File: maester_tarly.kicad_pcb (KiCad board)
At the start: 4 copper layers, 72 x 62.4 mm, 126 parts, among them J101 Micro_SD_Card_Det, J102 USB_B_Micro, J103 USB_A, J104 Conn_01x06, J105 Conn_01x10, J106 RJ45_Amphenol_RJMG1BD3B8K1ANR, J107 DF40GB(1.5)-48DS-0.4V, J108 DF40GB(1.5)-48DS-0.4V, J109 DF40GB(1.5)-48DS-0.4V, J110 DF40GB(1.5)-48DS-0.4V, U1 SAM9X60, U2 W971GG6SB-18, U3 MCP16501, U501 KSZ8081RNA, Y401 32.768kHz, Y402 DSC1001, Y501 DSC1001

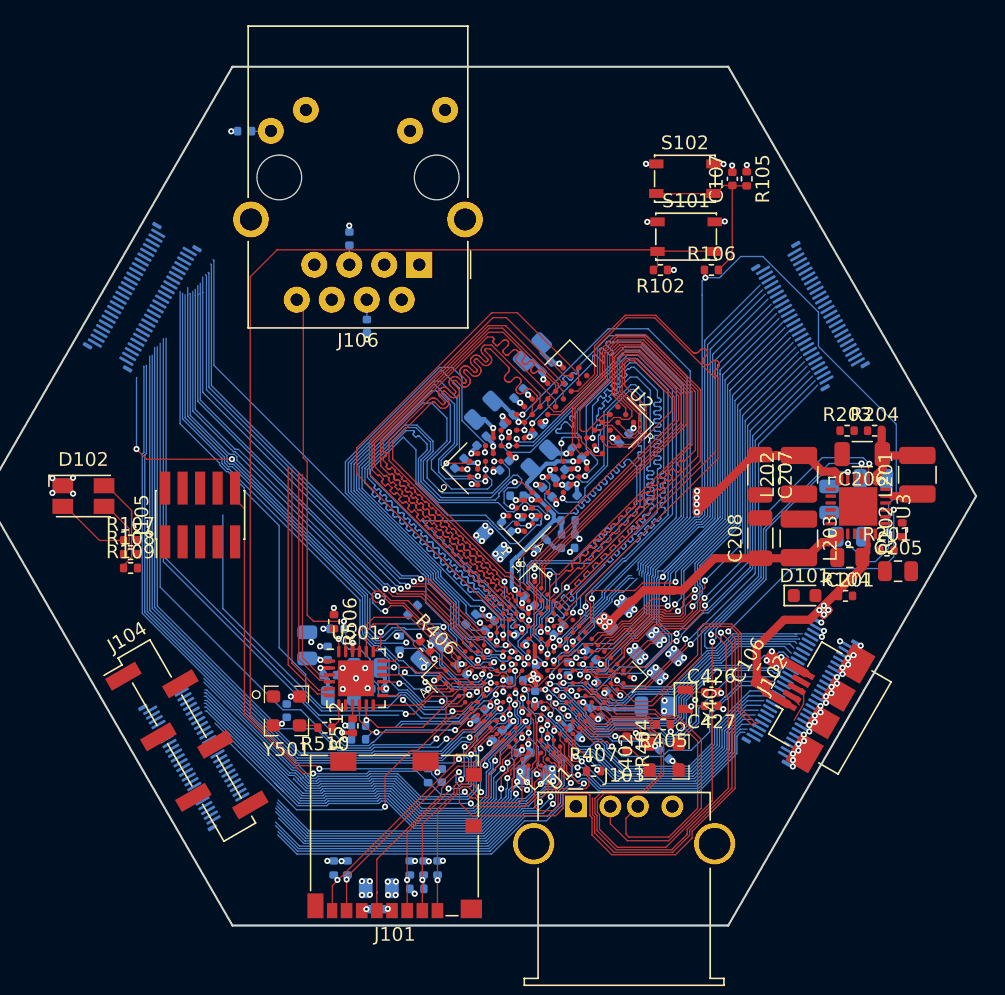
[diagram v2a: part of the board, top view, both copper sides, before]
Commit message: Routed power supply traces and vias. Repositioned mezzanine connectors.
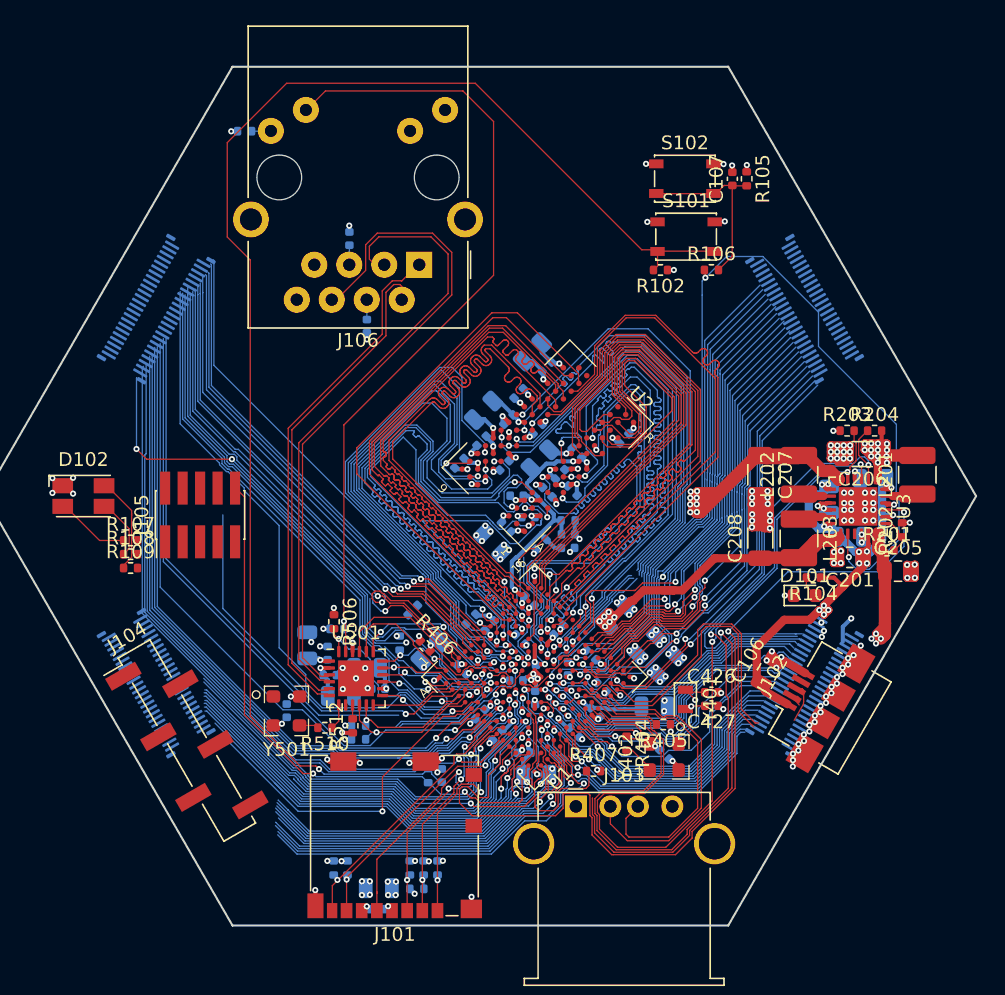
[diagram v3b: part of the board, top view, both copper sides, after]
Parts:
- moved J107 6.09 mm to (94.5, 144.8)
- moved R104 2.68 mm to (142.2, 137.1), turned to 180 degrees
- moved J109 1.33 mm to (94.5, 117.6)
- moved J110 0.67 mm to (141.5, 117.6)
- moved J108 0.66 mm to (141.5, 144.8)
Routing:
- net /ldo_out: track 0.00 -> 75.9 mm, vias 0 -> 4
- net GND: track 72.4 -> 129.1 mm, vias 126 -> 188
- net /a24: track 52.9 -> 15.1 mm
- net /a23: track 55.4 -> 92.9 mm
- net +5V: track 105.3 -> 139.7 mm, vias 4 -> 15
- net /CPU_IO/CPU_ETH_RX_N: track 15.9 -> 48.9 mm
- net /CPU_IO/CPU_ETH_LED: track 28.6 -> 58.8 mm
- net /CPU_IO/CPU_ETH_RX_P: track 16.4 -> 45.5 mm
- net /CPU_IO/CPU_ETH_TX_P: track 18.1 -> 37.2 mm
- net Net-(C105-Pad1): track 84.0 -> 102.5 mm
- net /CPU_IO/CPU_ETH_TX_N: track 17.7 -> 35.7 mm
- net +1.8V: track 50.7 -> 67.9 mm, vias 28 -> 32
- net +1.15V: track 41.4 -> 51.1 mm, vias 7 -> 9
- net +3V3: track 36.4 -> 45.9 mm, vias 50 -> 64
- net Net-(L202-Pad1): track 0.00 -> 3.52 mm
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
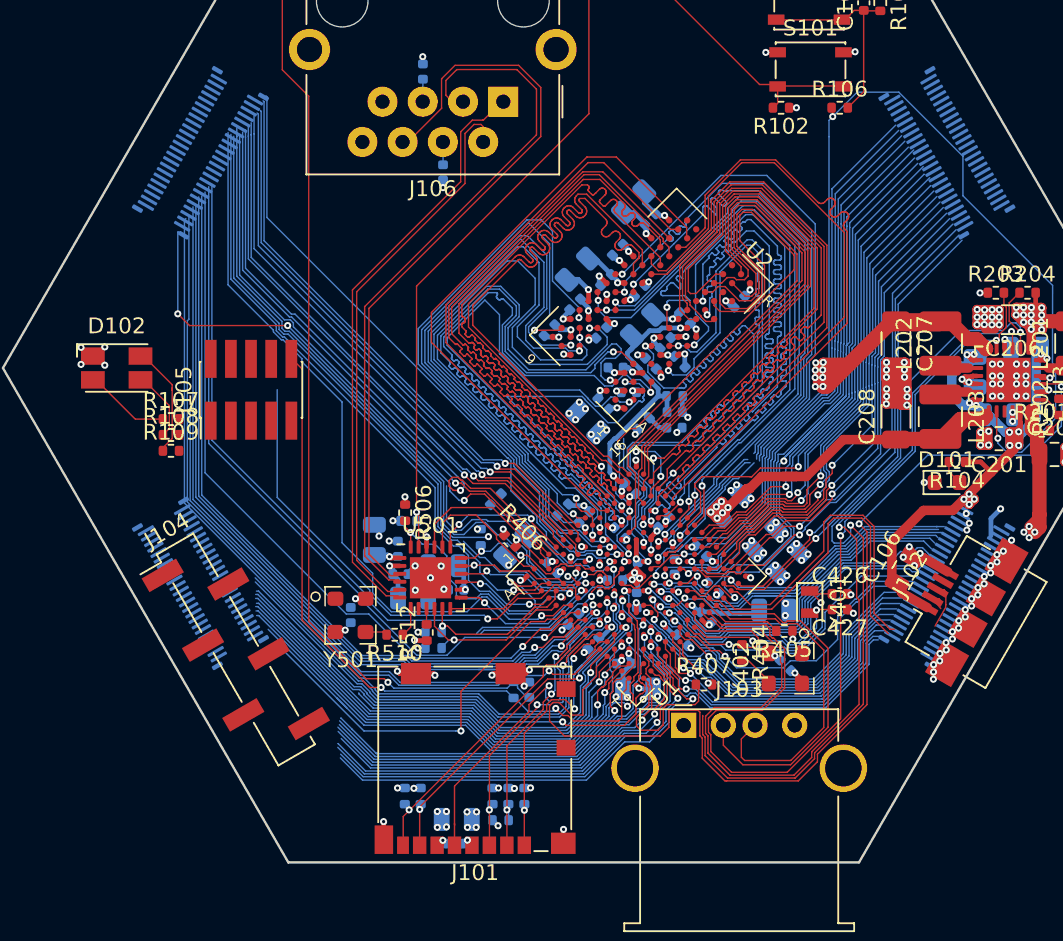
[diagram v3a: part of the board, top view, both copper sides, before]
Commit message: Wired up J107 and J109
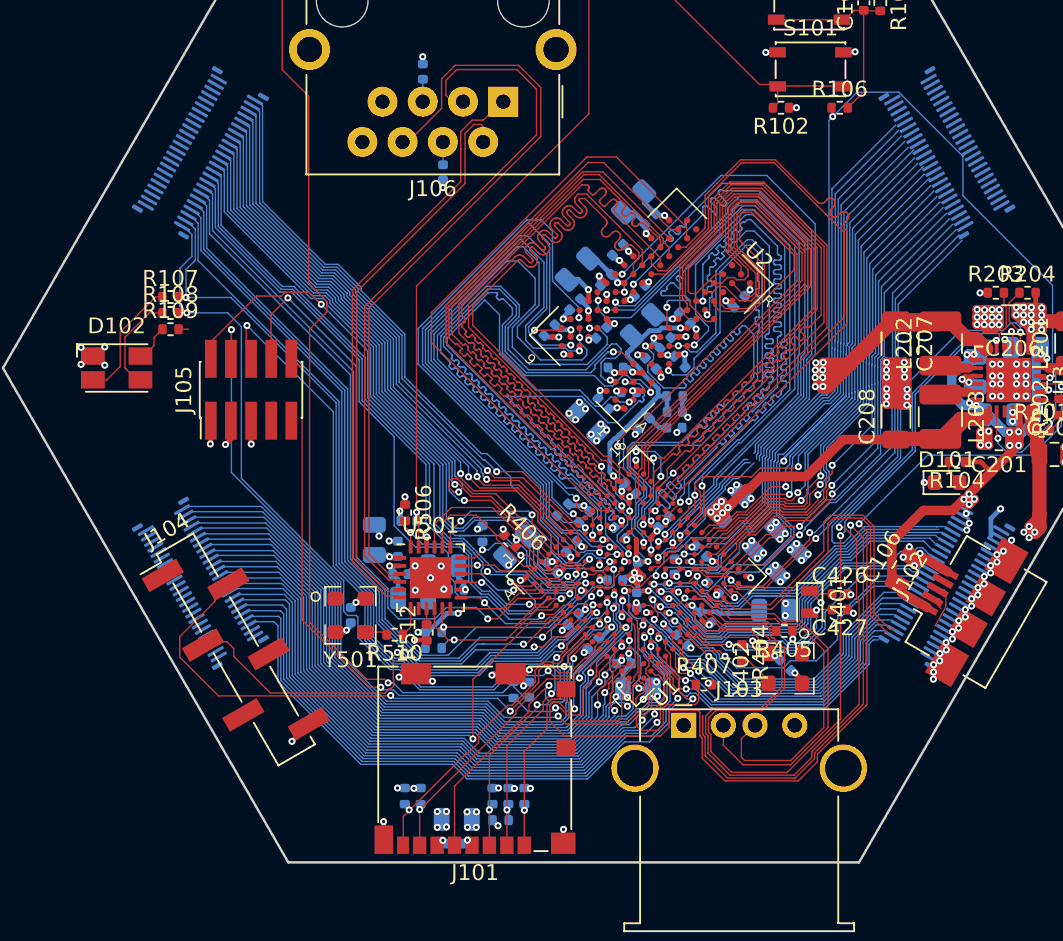
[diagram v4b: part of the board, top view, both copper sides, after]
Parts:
- moved R107 7.70 mm to (92.6, 126.7)
- moved R108 7.69 mm to (92.6, 127.7)
- moved R109 7.67 mm to (92.6, 128.7)
- moved C424 5.63 mm to (117.9, 142.4)
- moved R507 0.25 mm to (112.2, 141.6)
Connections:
- J107 pad 10: /c2 -> /c5
- J107 pad 12: /c3 -> /c7
- J107 pad 14: /c4 -> /c1
- J107 pad 16: /c5 -> /c3
- J107 pad 18: /c6 -> /c2
- J107 pad 20: /c7 -> /c6
- J107 pad 22: /c8 -> /c0
- J107 pad 24: /c9 -> /c4
- J107 pad 26: /a21 -> /a28
- J107 pad 28: /a14 -> /a7
- J107 pad 30: /a13 -> /a1
- J107 pad 32: /a12 -> /a2
- J107 pad 34: /a7 -> /a0
- J107 pad 36: /a6 -> /a4
- J107 pad 38: /a5 -> /a6
- J107 pad 40: /a4 -> /a13
- J107 pad 44: /a2 -> /a5
- J107 pad 46: /a1 -> /a14
- J107 pad 48: /a0 -> /a23
- J107 pad 6: /c0 -> /c12
- J107 pad 8: /c1 -> /c9
- J108 pad 10: /c12 -> /c8
- J109 pad 12: /a26 -> /a30
- J109 pad 14: /a25 -> /a22
- J109 pad 16: /a24 -> /a26
- J109 pad 18: /a23 -> /b14
- J109 pad 2: /a31 -> /a12
- J109 pad 20: /a22 -> /b17
- J109 pad 22: /b11 -> /b12
- J109 pad 24: /b12 -> /a21
- J109 pad 26: /b13 -> /b18
- J109 pad 28: /b14 -> /a24
- J109 pad 30: /b15 -> /b16
- J109 pad 32: /b16 -> /b13
- J109 pad 34: /b17 -> /b15
- J109 pad 36: /b18 -> /b23
- J109 pad 38: /b19 -> /b20
- J109 pad 4: /a30 -> /a25
- J109 pad 40: /b20 -> /b19
- J109 pad 46: /b23 -> /b24
- J109 pad 48: /b24 -> /b11
- J109 pad 8: /a28 -> /a31
- R107 pad 2: /a12 -> /a25
- R108 pad 2: /a13 -> /a12
- R109 pad 2: /a14 -> /a23
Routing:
- net /a23: track 92.9 -> 40.8 mm
- net /a26: track 11.5 -> 50.3 mm
- net /CPU_IO/CPU_DBG_UART_TX: track 1.85 -> 35.8 mm, vias 0 -> 2
- net /a24: track 15.1 -> 43.6 mm
- net /CPU_CORE/CPU_JTAG_TMS: track 9.51 -> 37.5 mm, vias 1 -> 2
- net /CPU_IO/CPU_DBG_UART_RX: track 11.2 -> 32.8 mm, vias 1 -> 2
- net /CPU_CORE/CPU_JTAG_TCK: track 31.9 -> 49.5 mm, vias 1 -> 2
- net /a13: track 24.6 -> 41.6 mm
- net /c4: track 26.3 -> 40.0 mm
- net /c0: track 26.3 -> 39.6 mm
- net /c6: track 28.8 -> 41.8 mm
- net /c2: track 28.1 -> 40.8 mm
- net /c3: track 27.4 -> 39.9 mm
- net /c1: track 26.2 -> 38.7 mm
- net /c7: track 25.7 -> 37.6 mm
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
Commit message: 27 Unrouted traces remaiin.
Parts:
- moved J104 48.6 mm to (124.7, 109.2), turned to 0 degrees
- moved R109 3.19 mm to (92.6, 131.9), turned to 270 degrees
- turned C428 to 135 degrees
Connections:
- J108 pad 10: /c8 -> /c23
- J108 pad 12: /c13 -> /c28
- J108 pad 14: /c14 -> /c25
- J108 pad 16: /c15 -> /c27
- J108 pad 18: /c16 -> /c17
- J108 pad 20: /c17 -> /c21
- J108 pad 22: /c18 -> /c8
- J108 pad 24: /c19 -> /c20
- J108 pad 26: /c20 -> /c26
- J108 pad 28: /c21 -> /c19
- J108 pad 30: /c22 -> /c13
- J108 pad 32: /c23 -> /c24
- J108 pad 34: /c24 -> /c15
- J108 pad 36: /c25 -> /c10
- J108 pad 38: /c26 -> /c22
- J108 pad 40: /c27 -> /c30
- J108 pad 42: /c28 -> /c18
- J108 pad 44: /c29 -> /c16
- J108 pad 46: /c30 -> /c14
- J108 pad 48: /c31 -> /c11
- J108 pad 6: /c10 -> /c31
- J108 pad 8: /c11 -> /c29
- J110 pad 10: /d2 -> /d11
- J110 pad 12: /d3 -> /d14
- J110 pad 14: /d4 -> /d20
- J110 pad 20: /d7 -> /d8
- J110 pad 22: /d8 -> /d13
- J110 pad 24: /d9 -> /d10
- J110 pad 26: /d10 -> /d12
- J110 pad 28: /d11 -> /d7
- J110 pad 30: /d12 -> /d15
- J110 pad 32: /d13 -> /d21
- J110 pad 34: /d14 -> /d17
- J110 pad 36: /d15 -> /d3
- J110 pad 38: /d16 -> /d19
- J110 pad 40: /d17 -> /d2
- J110 pad 42: /d18 -> /d4
- J110 pad 44: /d19 -> /d16
- J110 pad 46: /d20 -> /d1
- J110 pad 48: /d21 -> /d0
- J110 pad 6: /d0 -> /d9
- J110 pad 8: /d1 -> /d18
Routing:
- net /start_btn: track 75.0 -> 182.6 mm, vias 3 -> 4
- net GND: track 135.9 -> 214.2 mm, vias 191 -> 275
- net /CPU_IO/CPU_DBG_UART_RX: track 32.8 -> 107.7 mm
- net /CPU_IO/CPU_DBG_UART_TX: track 35.8 -> 107.4 mm
- net /d7: track 1.37 -> 35.8 mm, vias 0 -> 1
- net /periph_reset: track 15.0 -> 39.2 mm, vias 2 -> 4
- net /d5: track 58.3 -> 41.8 mm
- net /CPU_IO/CPU_ETH_TX_P: track 37.2 -> 51.9 mm
- net /CPU_IO/CPU_ETH_TX_N: track 35.7 -> 50.0 mm
- net /cpu_reset: track 97.0 -> 109.8 mm
- net /ldo_out: track 75.9 -> 85.4 mm, vias 4 -> 6
- net /a23: track 40.8 -> 48.6 mm, vias 1 -> 2
- net /CPU_CORE/CPU_USB_HOST_P: track 23.4 -> 30.0 mm
- net /CPU_IO/CPU_ETH_RX_P: track 45.5 -> 50.0 mm
- net /CPU_CORE/CPU_USB_HOST_N: track 21.6 -> 26.1 mm
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
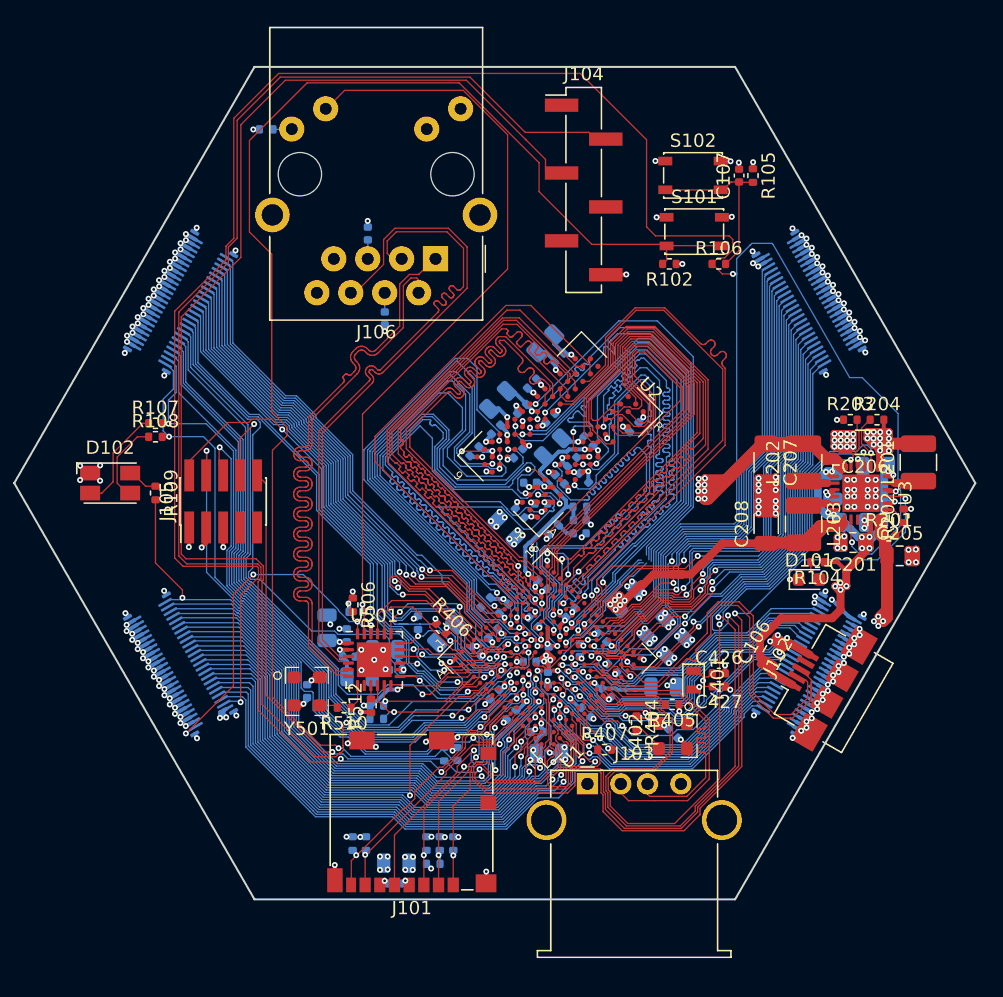
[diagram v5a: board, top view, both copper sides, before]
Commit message: Cleaned silkscreen, routed all traces, USB-A and SD need rerouting, need to redo ram wiggles
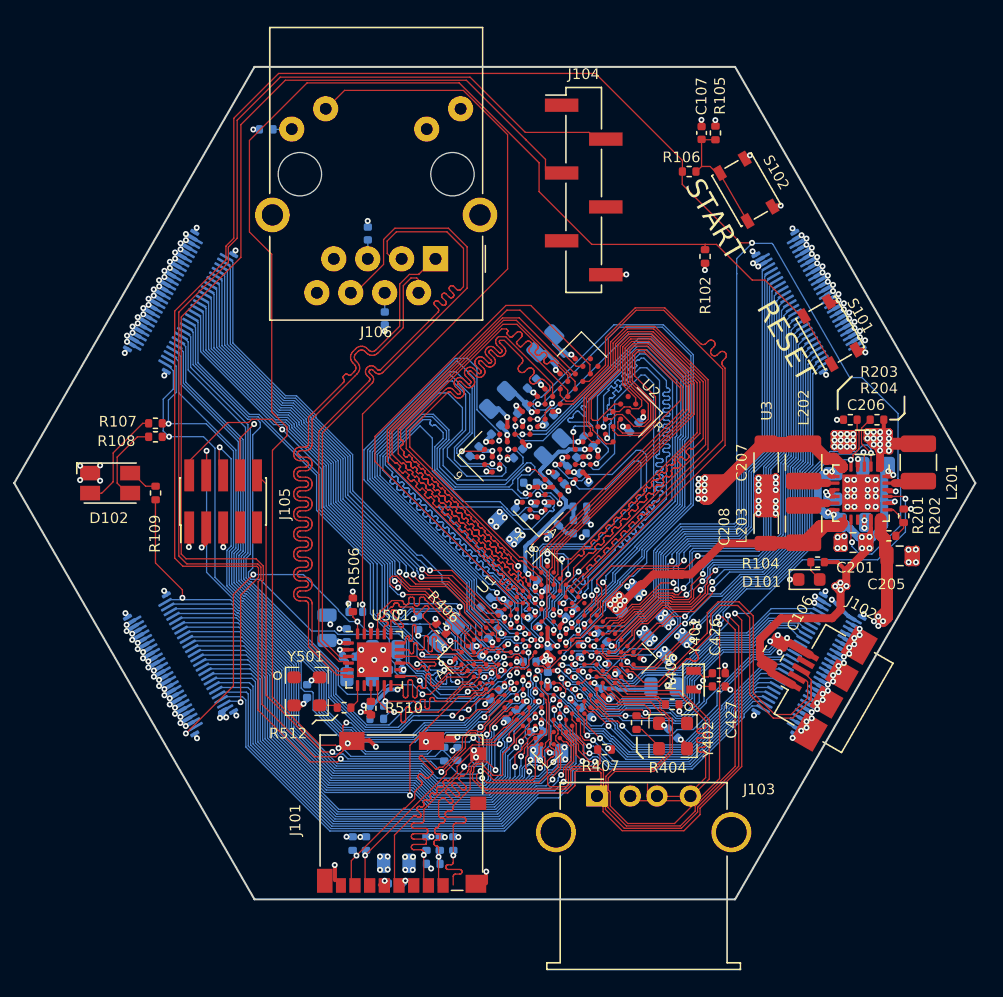
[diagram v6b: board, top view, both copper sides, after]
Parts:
- moved S101 12.7 mm to (143.1, 119.9), turned to 300 degrees
- moved R106 7.27 mm to (132.6, 107.8)
- moved C107 4.25 mm to (133.5, 105.0)
- moved R105 4.25 mm to (134.5, 105.0)
- moved S102 4.12 mm to (136.8, 109.2), turned to 300 degrees
- moved R102 2.73 mm to (133.8, 114.2), turned to 90 degrees
- moved J103 1.15 mm to (125.7, 154.6)
- moved J101 0.76 mm to (111.0, 155.9)
- moved R512 0.18 mm to (108.7, 148.0)
- moved C302 0.15 mm to (122.1, 126.4)
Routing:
- net Net-(C105-Pad1): track 105.0 -> 116.0 mm
- net /CPU_CORE/data6: track 36.5 -> 26.8 mm
- net /CPU_CORE/CPU_DDR_LOW_MASK: track 38.0 -> 28.7 mm
- net /mmcdat3: track 17.5 -> 24.1 mm
- net /start_btn: track 182.6 -> 176.4 mm
- net /CPU_IO/CPU_MMC_CMD: track 17.9 -> 23.7 mm
- net /CPU_IO/PHY_RXD1: track 6.28 -> 12.0 mm
- net /CPU_IO/PHY_RXDV: track 6.35 -> 12.1 mm
- net /CPU_IO/PHY_RXER: track 6.94 -> 12.0 mm, vias 1 -> 0
- net /mmcdat2: track 20.4 -> 24.8 mm
- net /CPU_CORE/data2: track 40.7 -> 45.1 mm
- net Net-(C107-Pad1): track 13.4 -> 9.07 mm
- net /CPU_IO/PHY_CLK: track 7.72 -> 11.9 mm
- net /mmcdat1: track 19.5 -> 23.5 mm
- net /CPU_CORE/data4: track 38.0 -> 34.3 mm
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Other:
- board text added: "RESET"
- board text added: "START"
